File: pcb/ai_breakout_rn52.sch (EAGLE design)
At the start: 8 parts, among them IC1 RN-52, J1 1X20, J2 1X20

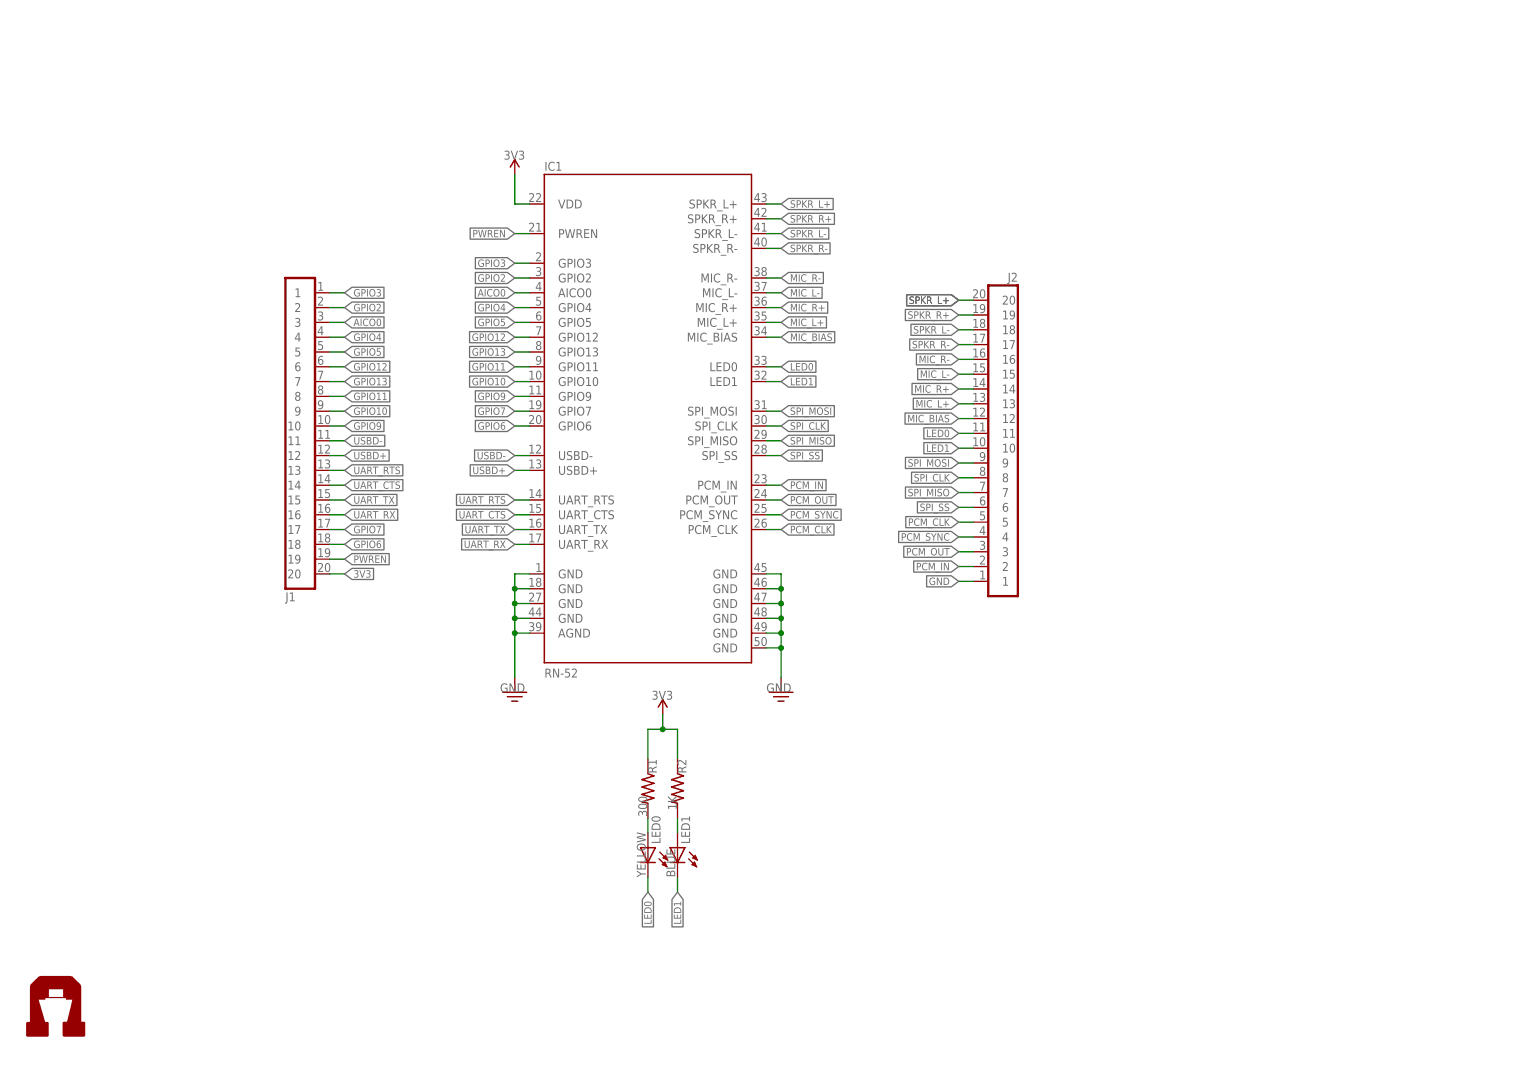
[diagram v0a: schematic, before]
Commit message: New breaboardable version.
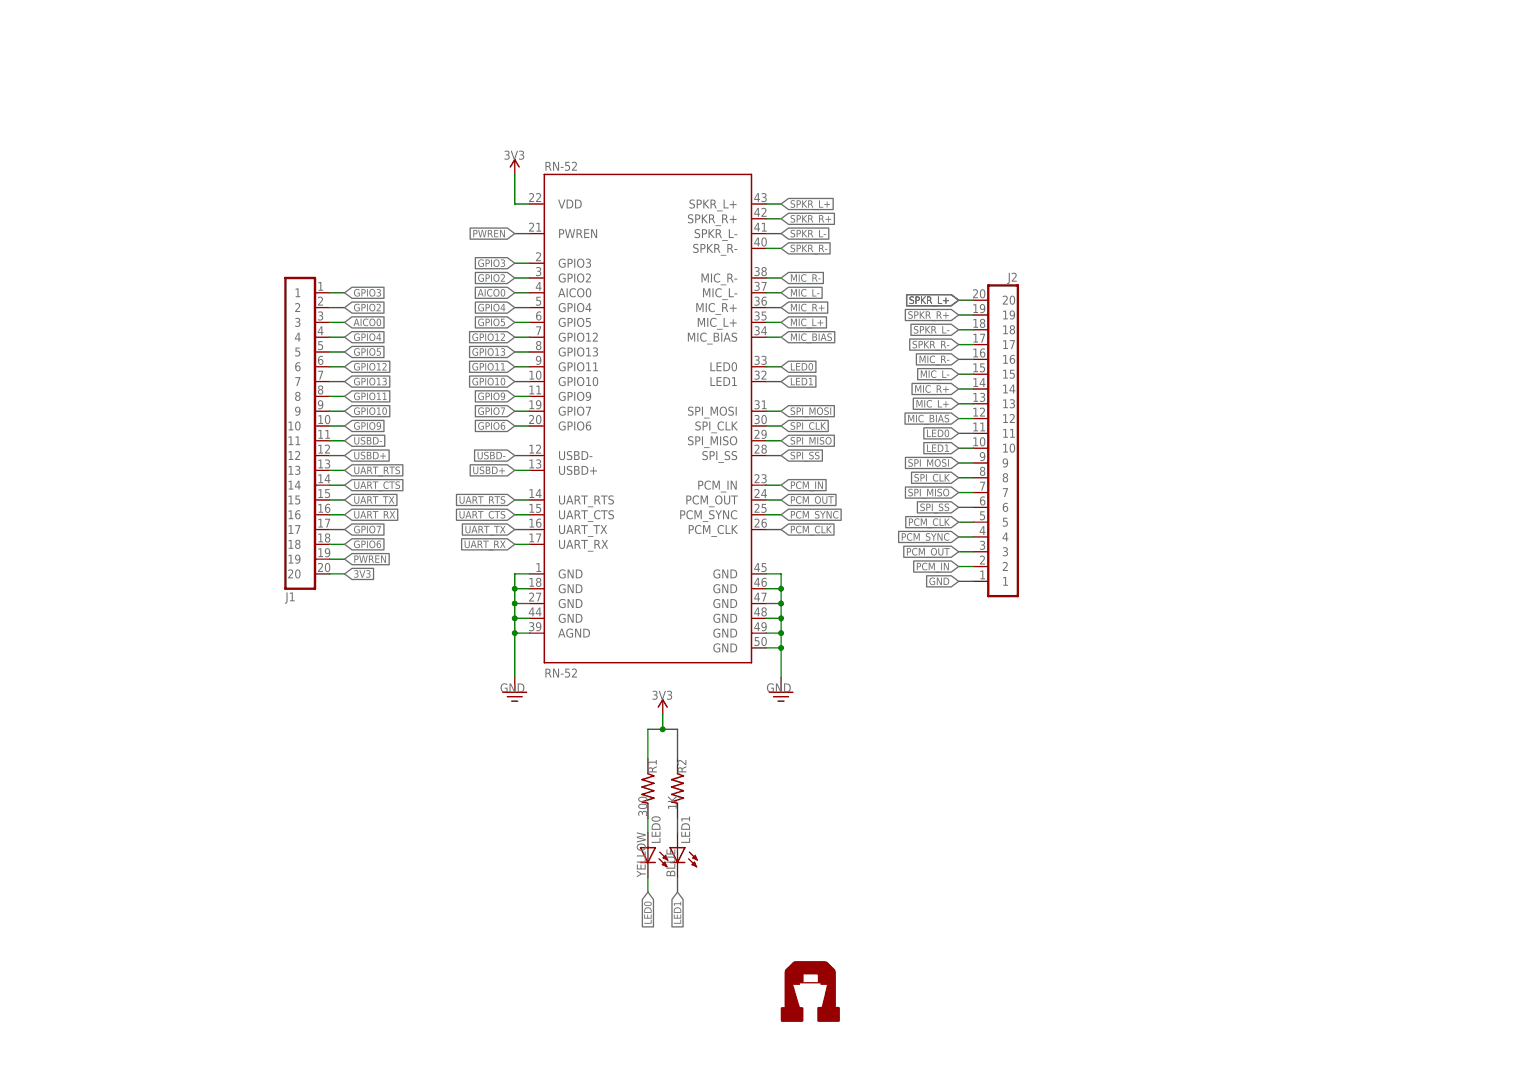
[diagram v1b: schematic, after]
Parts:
- renumbered IC1 to RN-52

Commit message: updating
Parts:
- added FRAME1: FRAME-LETTER, Ai_Miscellany:FRAME-LETTER
- RN-52: value RN-52 -> RN52; device Ai_IC:RN-52 -> Ai_RF:RN52
- U$3: value AI-LOGOL -> AI-LOGOXS; device Ai_Miscellany:AI-LOGOL -> Ai_Miscellany:AI-LOGOXS
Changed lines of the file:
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@@
 <?xml version="1.0" encoding="utf-8"?>
 <!DOCTYPE eagle SYSTEM "eagle.dtd">
-<eagle version="6.5.0">
+<eagle version="7.1.0">
 <drawing>
 <settings>
@@
 <setting verticaltext="up"/>
 </settings>
-<grid distance="0.1" unitdist="inch" unit="inch" style="lines" multiple="1" display="no" altdistance="0.01" altunitdist="inch" altunit="inch"/>
+<grid distance="50" unitdist="mil" unit="mil" style="lines" multiple="1" display="yes" altdistance="0.01" altunitdist="inch" altunit="inch"/>
 <layers>
 <layer number="1" name="Top" color="4" fill="1" visible="no" active="no"/>
@@
 <layer number="56" name="wert" color="7" fill="1" visible="no" active="no"/>
 <layer number="57" name="tCAD" color="7" fill="1" visible="no" active="no"/>
+<layer number="59" name="tCarbon" color="7" fill="1" visible="no" active="no"/>
+<layer number="60" name="bCarbon" color="7" fill="1" visible="no" active="no"/>
+<layer number="90" name="Modules" color="5" fill="1" visible="yes" active="yes"/>
 <layer number="91" name="Nets" color="2" fill="1" visible="yes" active="yes"/>
 <layer number="92" name="Busses" color="1" fill="1" visible="yes" active="yes"/>
@@
 <layer number="97" name="Info" color="7" fill="1" visible="yes" active="yes"/>
 <layer number="98" name="Guide" color="6" fill="1" visible="yes" active="yes"/>
+<layer number="99" name="SpiceOrder" color="7" fill="1" visible="no" active="no"/>
 <layer number="100" name="Muster" color="7" fill="1" visible="no" active="no"/>
 <layer number="101" name="Patch_Top" color="12" fill="4" visible="yes" active="yes"/>
@@
 <layer number="112" name="tSilk" color="7" fill="1" visible="yes" active="yes"/>
 <layer number="113" name="Route13" color="7" fill="1" visible="no" active="no"/>
+<layer number="114" name="Badge_Outline" color="7" fill="1" visible="yes" active="yes"/>
+<layer number="115" name="ReferenceISLANDS" color="7" fill="1" visible="yes" active="yes"/>
 <layer number="116" name="Patch_BOT" color="9" fill="4" visible="yes" active="yes"/>
 <layer number="117" name="mPads" color="7" fill="1" visible="no" active="no"/>
@@
 <layer number="223" name="223bmp" color="24" fill="1" visible="no" active="no"/>
 <layer number="224" name="224bmp" color="25" fill="1" visible="no" active="no"/>
+<layer number="225" name="225bmp" color="7" fill="1" visible="yes" active="yes"/>
+<layer number="226" name="226bmp" color="7" fill="1" visible="yes" active="yes"/>
+<layer number="227" name="227bmp" color="7" fill="1" visible="yes" active="yes"/>
+<layer number="228" name="228bmp" color="7" fill="1" visible="yes" active="yes"/>
+<layer number="229" name="229bmp" color="7" fill="1" visible="yes" active="yes"/>
+<layer number="230" name="230bmp" color="7" fill="1" visible="yes" active="yes"/>
+<layer number="231" name="231bmp" color="7" fill="1" visible="yes" active="yes"/>
 <layer number="248" name="Housing" color="7" fill="1" visible="yes" active="yes"/>
 <layer number="249" name="Edge" color="7" fill="1" visible="yes" active="yes"/>
@@
 <layer number="251" name="SMDround" color="7" fill="1" visible="no" active="no"/>
 <layer number="254" name="cooling" color="7" fill="1" visible="yes" active="yes"/>
+<layer number="255" name="routoute" color="7" fill="1" visible="yes" active="yes"/>
 </layers>
 <schematic xreflabel="%F%N/%S.%C%R" xrefpart="/%S.%C%R">
@@
 <parts>
 <part name="FRAME1" library="Ai_Miscellany" deviceset="FRAME-LETTER" device="">
-<attribute name="AUTHOR" value="A.I. HARDWARE SITH LORDS"/>
-<attribute name="REV" value="1.0"/>
+<attribute name="REV" value="1.1"/>
 </part>
 <part name="LED0" library="Ai_LED" deviceset="LED" device="0603" value="YELLOW"/>
@@
 <part name="J2" library="Ai_Connectors" deviceset="1X20" device=""/>
 <part name="J1" library="Ai_Connectors" deviceset="1X20" device=""/>
-<part name="RN-52" library="Ai_IC" deviceset="RN-52" device=""/>
+<part name="RN-52" library="Ai_RF" deviceset="RN52" device=""/>
 <part name="GND1" library="Ai_Power" deviceset="GND" device=""/>
 <part name="GND2" library="Ai_Power" deviceset="GND" device=""/>
-<part name="U$3" library="Ai_Miscellany" deviceset="AI-LOGO" device="L"/>
+<part name="U$3" library="Ai_Miscellany" deviceset="AI-LOGO" device="XS" value="AI-LOGOXS"/>
 </parts>
 <sheets>
@@
 <instances>
 <instance part="FRAME1" gate="G$1" x="0" y="0"/>
-<instance part="FRAME1" gate="G$2" x="147.32" y="0">
-<attribute name="AUTHOR" x="147.32" y="0" size="1.778" layer="96" display="off"/>
-<attribute name="REV" x="147.32" y="0" size="1.778" layer="96" display="off"/>
+<instance part="FRAME1" gate="G$2" x="154.94" y="3.81">
+<attribute name="REV" x="154.94" y="3.81" size="1.778" layer="96" display="off"/>
 </instance>
 <instance part="LED0" gate="G$1" x="109.22" y="35.56" rot="MR0"/>
@@
 <instance part="GND1" gate="GND" x="132.08" y="62.23"/>
 <instance part="GND2" gate="GND" x="86.36" y="62.23"/>
-<instance part="U$3" gate="G$1" x="137.16" y="10.16"/>
+<instance part="U$3" gate="G$1" x="146.05" y="19.05"/>
 </instances>
 <busses>
@@
 </schematic>
 </drawing>
+<compatibility>
+<note version="6.3" minversion="6.2.2" severity="warning">
+Since Version 6.2.2 text objects can contain more than one line,
+which will not be processed correctly with this version.
+</note>
+</compatibility>
 </eagle>
